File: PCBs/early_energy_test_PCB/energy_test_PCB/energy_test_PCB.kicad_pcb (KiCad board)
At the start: 2 copper layers, 120 x 56.8 mm, 31 parts, among them J1 B2B-PH-K-S_LF__SN_, J2 B2B-PH-K-S_LF__SN_, J3 B2B-PH-K-S_LF__SN_, U1 IRLML6244TRPBF, U3 LTC4071EMS8E_PBF

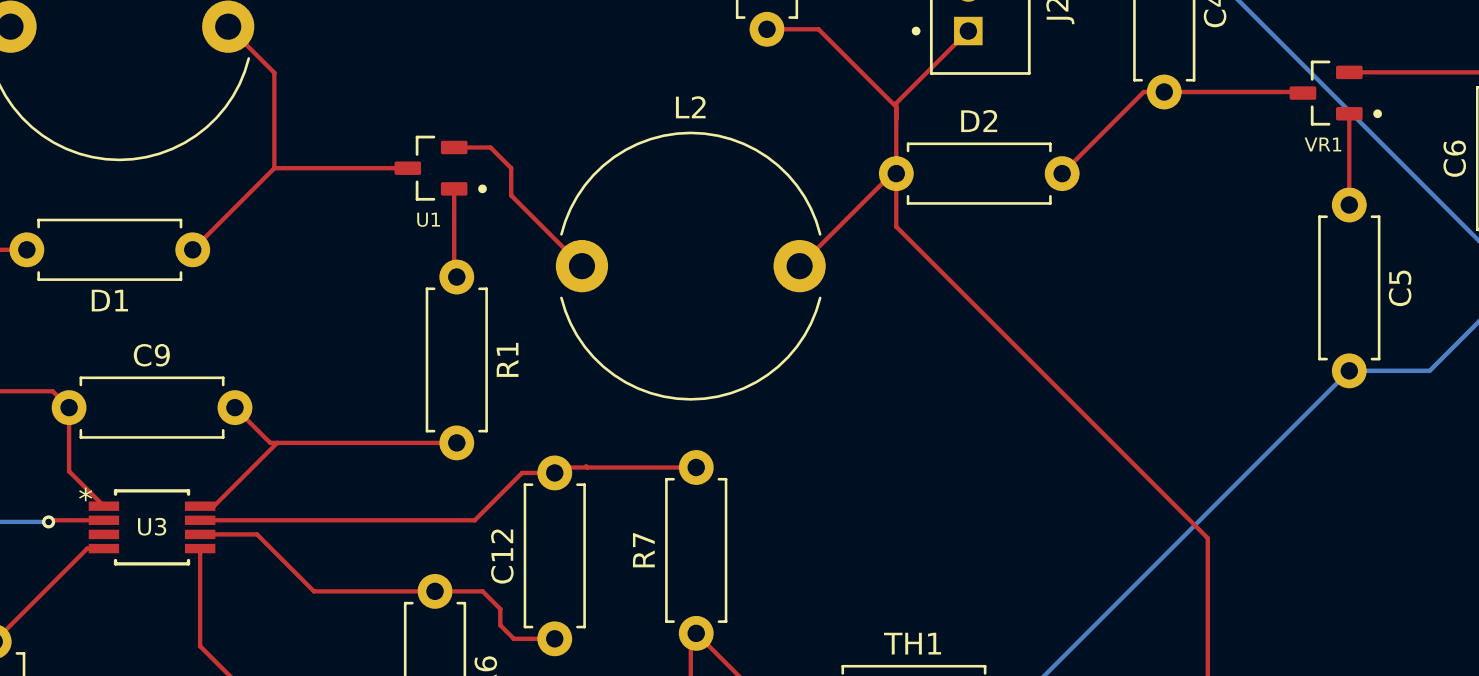
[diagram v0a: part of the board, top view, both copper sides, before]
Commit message: add the 3rd pcb
Added new connector footprints, symbols, and STEP models for 2N2222, 2N2222A, BPW34, and 657002140201 in main_PCB_V1. Created new connector PCB project files. Updated .gitignore to exclude new backup and gerber directories. Modified early_energy_test_PCB to output gerbers to a dedicated folder and made minor PCB net and property adjustments.
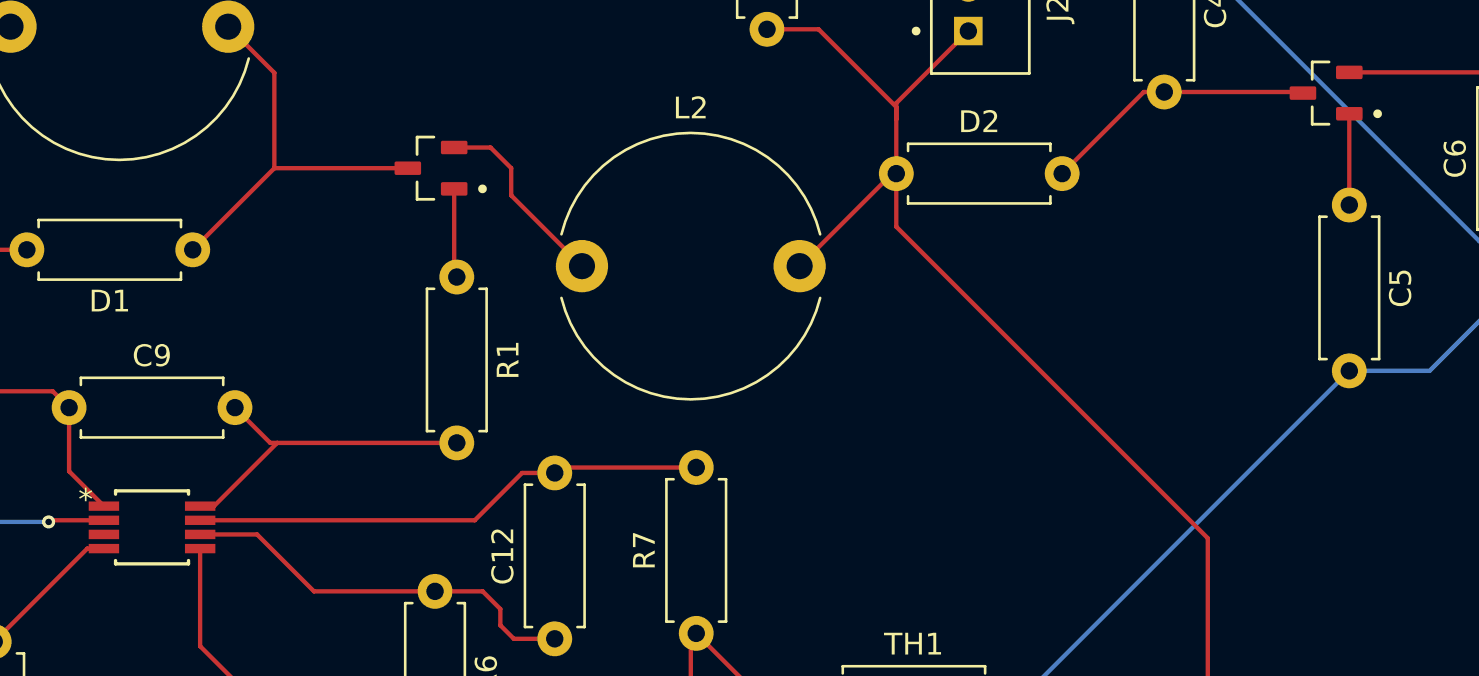
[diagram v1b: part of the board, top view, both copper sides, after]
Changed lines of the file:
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@@
 		(pcbplotparams
 			(layerselection 0x00000000_00000000_55555555_5755f5ff)
-			(plot_on_all_layers_selection 0x00000000_00000000_00000000_00000000)
+			(plot_on_all_layers_selection 0x00000000_00000000_00000000_0200a0af)
 			(disableapertmacros no)
-			(usegerberextensions no)
+			(usegerberextensions yes)
 			(usegerberattributes yes)
 			(usegerberadvancedattributes yes)
@@
 			(outputformat 1)
 			(mirror no)
-			(drillshape 1)
+			(drillshape 0)
 			(scaleselection 1)
-			(outputdirectory "")
+			(outputdirectory "gerber/")
 		)
 	)
@@
 			(at 0.107 -2.3864 0)
 			(layer "F.SilkS")
+			(hide yes)
 			(effects
 				(font
@@
 			(at 0.107 -2.3864 0)
 			(layer "F.SilkS")
+			(hide yes)
 			(effects
 				(font
@@
 			(at 0 0 0)
 			(layer "F.SilkS")
+			(hide yes)
 			(effects
 				(font
@@
 			(at 0 0 0)
 			(layer "F.Fab")
+			(hide yes)
 			(effects
 				(font
@@
 	)
 	(segment
-		(start 128 137.5)
-		(end 125.825 139.675)
+		(start 129.75 137.25)
+		(end 129.5 137.5)
 		(width 0.2)
 		(layer "F.Cu")
@@
 	)
 	(segment
-		(start 129.75 137.25)
-		(end 129.5 137.5)
+		(start 128 137.5)
+		(end 125.825 139.675)
 		(width 0.2)
 		(layer "F.Cu")
@@
 		(width 0.2)
 		(layer "F.Cu")
-		(net 11)
-	)
-	(segment
-		(start 131 137.25)
-		(end 130.94 137.19)
-		(width 0.2)
-		(layer "F.Cu")
